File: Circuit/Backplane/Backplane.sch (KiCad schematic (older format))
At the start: 67 parts, among them CON1 peripheral_bridge, CON2 power_distributor, J1 USB_OTG, J2 power_source_mode, J3 general_power_source, J4 pneumatic, J5 pressure_sensor, J6 RS232_DVL, P1 imaging_sonar, P2 DVL, P3 computer1, P4 computer2, P5 ethernet_switch, P6 general, U1 LM1117-3.3, U2 TUSB4041I, U3 TLV73311PDBVT, Y1 24MHz

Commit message: grouping component in pcb
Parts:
- J2, J3: footprint Pin_Headers:Pin_Header_Straight_1x03_Pitch2.54mm -> Zeabus:90136-2013
- J5, J6: footprint Zeabus:70543-0002 -> Zeabus:90136-2013
- renumbered L2 to L1, L4 to L2, L5 to L3, L1 to L4, L3 to L5

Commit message: Change DVL Footprint
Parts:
- J2, J3, J5, J6: footprint Zeabus:90136-2013 -> Zeabus:70543-0002
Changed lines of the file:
@@
 F 0 "J6" H 9700 4900 50  0000 C CNN
 F 1 "RS232_DVL" H 9700 4500 50  0000 C CNN
-F 2 "Zeabus:90136-2013" H 9700 4700 50  0001 C CNN
+F 2 "Zeabus:70543-0002" H 9700 4700 50  0001 C CNN
 F 3 "" H 9700 4700 50  0001 C CNN
 	1    9700 4700
@@
 F 0 "J5" H 9700 4450 50  0000 C CNN
 F 1 "pressure_sensor" H 9700 4050 50  0000 C CNN
-F 2 "Zeabus:90136-2013" H 9700 4250 50  0001 C CNN
+F 2 "Zeabus:70543-0002" H 9700 4250 50  0001 C CNN
 F 3 "" H 9700 4250 50  0001 C CNN
 	1    9700 4250
@@
 F 0 "J2" H 1050 5900 50  0000 C CNN
 F 1 "power_source_mode" H 1050 5500 50  0000 C CNN
-F 2 "Zeabus:90136-2013" H 1100 5700 50  0001 C CNN
+F 2 "Zeabus:70543-0002" H 1100 5700 50  0001 C CNN
 F 3 "" H 1100 5700 50  0001 C CNN
 	1    1050 5700
@@
 F 0 "J3" H 1050 6700 50  0000 C CNN
 F 1 "general_power_source" H 1050 6300 50  0000 C CNN
-F 2 "Zeabus:90136-2013" H 1100 6500 50  0001 C CNN
+F 2 "Zeabus:70543-0002" H 1100 6500 50  0001 C CNN
 F 3 "" H 1100 6500 50  0001 C CNN
 	1    1050 6500

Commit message: Jumper Footprint change to pinheader
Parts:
- J2, J3: footprint Zeabus:70543-0002 -> Pin_Headers:Pin_Header_Straight_1x03_Pitch2.54mm
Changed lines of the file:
@@
 F 0 "J2" H 1050 5900 50  0000 C CNN
 F 1 "power_source_mode" H 1050 5500 50  0000 C CNN
-F 2 "Zeabus:70543-0002" H 1100 5700 50  0001 C CNN
+F 2 "Pin_Headers:Pin_Header_Straight_1x03_Pitch2.54mm" H 1100 5700 50  0001 C CNN
 F 3 "" H 1100 5700 50  0001 C CNN
 	1    1050 5700
@@
 F 0 "J3" H 1050 6700 50  0000 C CNN
 F 1 "general_power_source" H 1050 6300 50  0000 C CNN
-F 2 "Zeabus:70543-0002" H 1100 6500 50  0001 C CNN
+F 2 "Pin_Headers:Pin_Header_Straight_1x03_Pitch2.54mm" H 1100 6500 50  0001 C CNN
 F 3 "" H 1100 6500 50  0001 C CNN
 	1    1050 6500

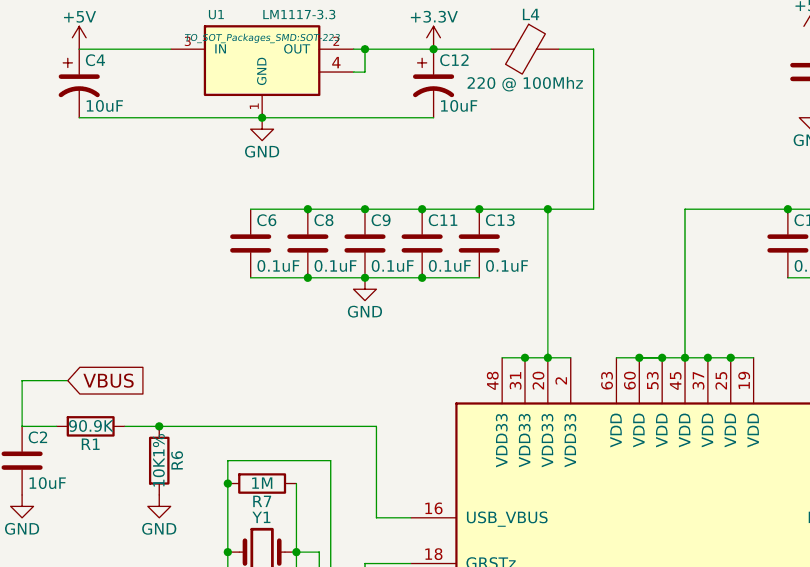
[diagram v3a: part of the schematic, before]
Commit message: changed value of capacitor that connected with VDD33 (0.1uF to 10uF)
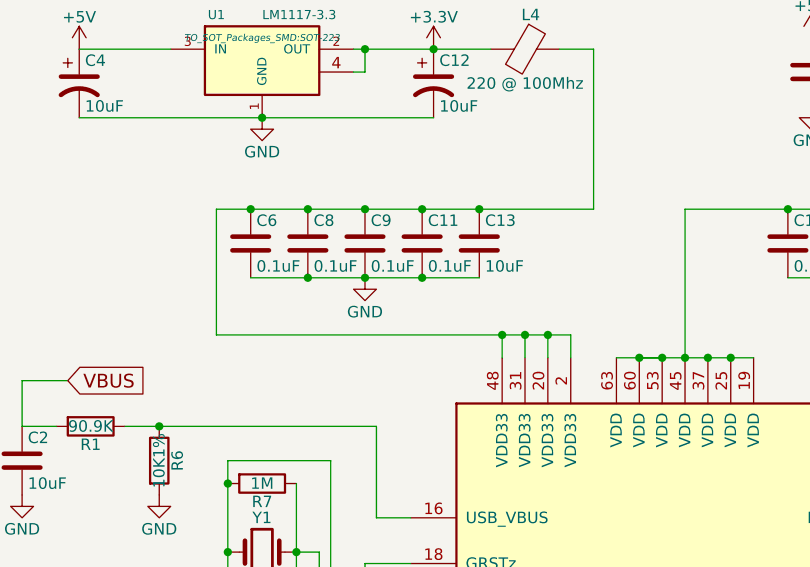
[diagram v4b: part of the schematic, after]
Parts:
- C13: value 0.1uF -> 10uF
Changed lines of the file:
@@
 P 3400 1850
 F 0 "C13" H 3425 1950 50  0000 L CNN
-F 1 "0.1uF" H 3425 1750 50  0000 L CNN
+F 1 "10uF" H 3425 1750 50  0000 L CNN
 F 2 "Capacitors_SMD:C_0603_HandSoldering" H 3438 1700 50  0001 C CNN
 F 3 "" H 3400 1850 50  0001 C CNN
@@
 	3100 3950 3100 4050
 Wire Wire Line
-	3500 2350 3800 2350
-Connection ~ 3600 2350
-Connection ~ 3700 2350
-Wire Wire Line
-	3700 1700 3700 2350
-Wire Wire Line
 	4000 2350 4600 2350
 Connection ~ 4100 2350
@@
 	4300 1700 4300 2350
 Wire Wire Line
-	2400 1700 3900 1700
+	2250 1700 3900 1700
 Connection ~ 2650 1700
 Connection ~ 2900 1700
@@
 Wire Wire Line
 	3900 1000 3900 1700
-Connection ~ 3700 1700
 Wire Wire Line
 	11050 1600 11250 1600
+Wire Wire Line
+	3800 2350 3800 2250
+Wire Wire Line
+	3800 2250 2250 2250
+Wire Wire Line
+	2250 2250 2250 1700
+Connection ~ 2400 1700
+Wire Wire Line
+	3700 2350 3700 2250
+Connection ~ 3700 2250
+Wire Wire Line
+	3600 2350 3600 2250
+Connection ~ 3600 2250
+Wire Wire Line
+	3500 2350 3500 2250
+Connection ~ 3500 2250
 $EndSCHEMATC

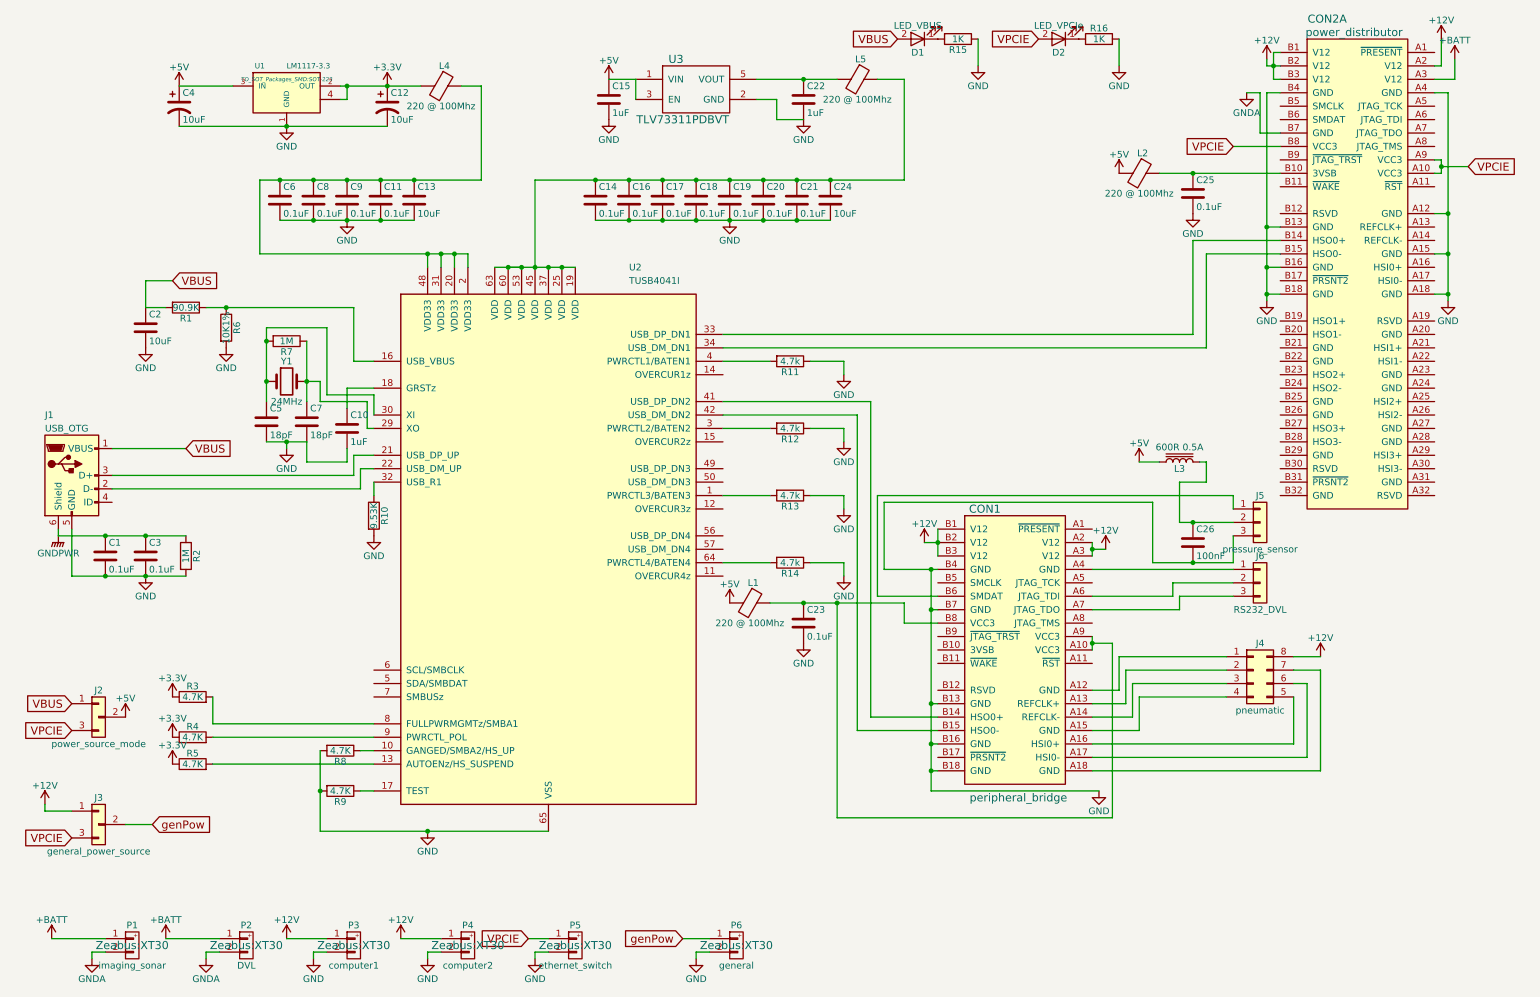
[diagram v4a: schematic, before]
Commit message: Add LEDS
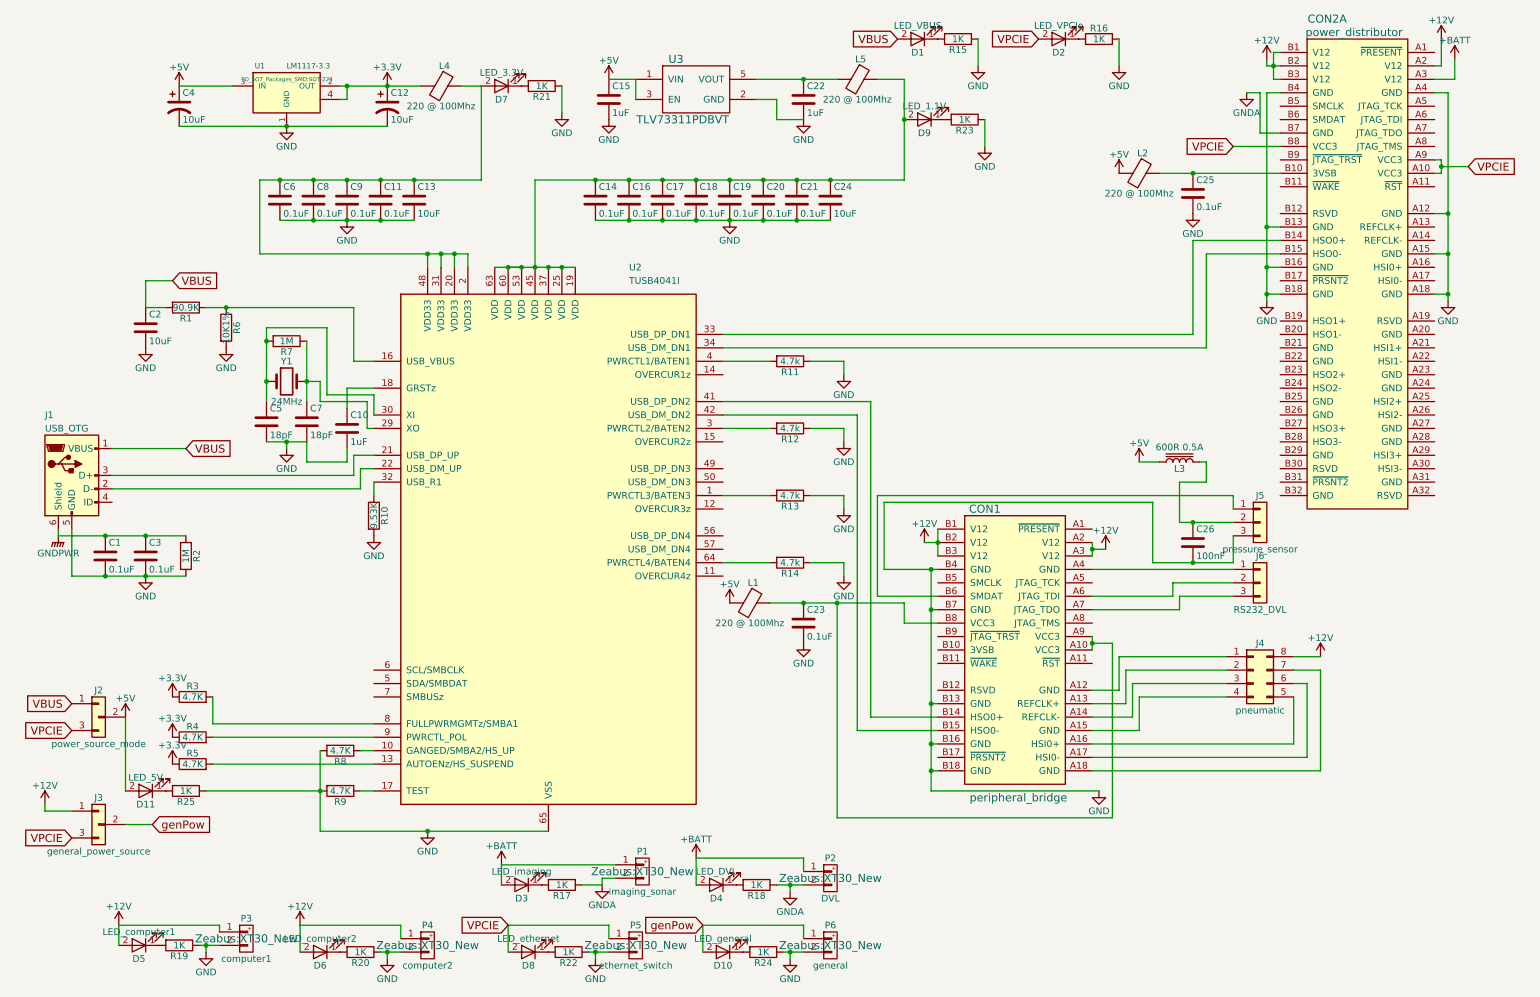
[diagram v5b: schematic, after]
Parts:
- added D10: LED_general, LEDs:LED_0603_HandSoldering, symbol LED
- added D11: LED_5V, LEDs:LED_0603_HandSoldering, symbol LED
- added D3: LED_imaging, LEDs:LED_0603_HandSoldering, symbol LED
- added D4: LED_DVL, LEDs:LED_0603_HandSoldering, symbol LED
- added D5: LED_computer1, LEDs:LED_0603_HandSoldering, symbol LED
- added D6: LED_computer2, LEDs:LED_0603_HandSoldering, symbol LED
- added D7: LED_3.3V, LEDs:LED_0603_HandSoldering, symbol LED
- added D8: LED_ethernet, LEDs:LED_0603_HandSoldering, symbol LED
- added D9: LED_1.1V, LEDs:LED_0603_HandSoldering, symbol LED
- added R17, R18, R19, R20, R21, R22, R23, R24, R25: 1K, Resistors_SMD:R_0603_HandSoldering, symbol R
- P1, P2, P3, P4, P5, P6: footprint Zeabus:XT30 -> Zeabus:XT30_New
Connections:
- net +12V: now also D5.2 (A), D6.2 (A)
- net +5V: now also D11.2 (A)
- net +BATT: now also D3.2 (A), D4.2 (A)
- net GND: now also R19.1, R20.1, R21.1, R22.1, R23.1, R24.1, R25.1
- net GNDA: now also R17.1, R18.1
- net VPCIE: now also D8.2 (A)
- net genPow: now also D10.2 (A)
- net at C14.1, C16.1, C17.1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: now also D9.2 (A)
- net at C11.1, C13.1, C6.1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: now also D7.2 (A)
- new net: D7.1 (K), R21.2
- new net: D9.1 (K), R23.2
- new net: D3.1 (K), R17.2
- new net: D5.1 (K), R19.2
- new net: D4.1 (K), R18.2
- new net: D6.1 (K), R20.2
- new net: D8.1 (K), R22.2
- new net: D10.1 (K), R24.2
- new net: D11.1 (K), R25.2
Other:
- moved on the sheet: P1, P2, P3, P4, P5, P6

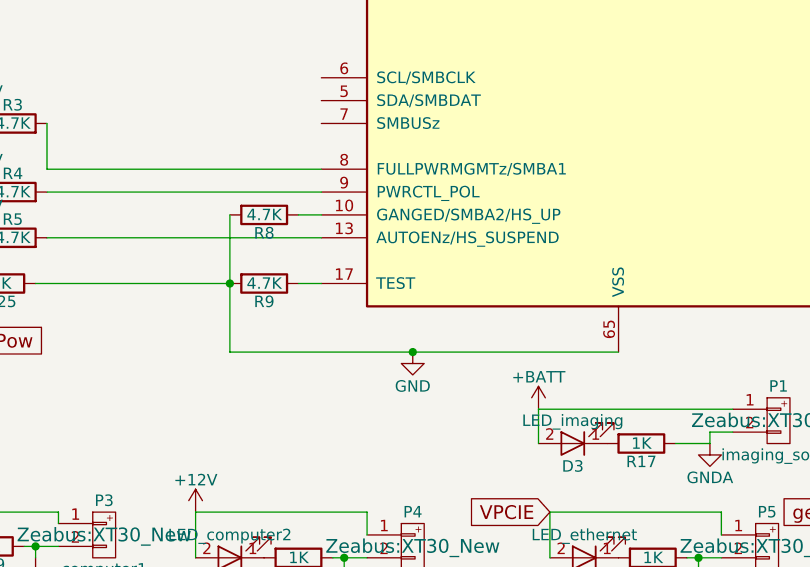
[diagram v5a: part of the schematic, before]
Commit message: relocated component in pcb
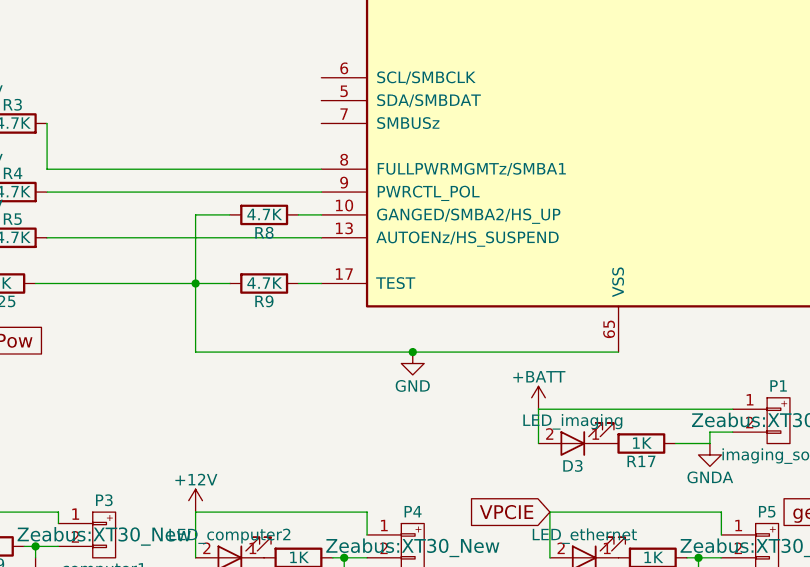
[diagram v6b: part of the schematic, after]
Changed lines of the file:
@@
 	6600 4550 6600 4650
 Wire Wire Line
-	2700 6550 4400 6550
+	2550 6550 4400 6550
 Wire Wire Line
 	3100 5950 3000 5950
@@
 	1900 5750 1900 5550
 Connection ~ 7250 4600
-Wire Wire Line
-	2700 5950 2700 6550
-Connection ~ 2700 6250
 Wire Wire Line
 	3100 3450 3100 3300
@@
 	1    0    0    -1
 $EndComp
+Wire Wire Line
+	2700 5950 2550 5950
+Wire Wire Line
+	2550 5950 2550 6550
+Connection ~ 2550 6250
 $EndSCHEMATC

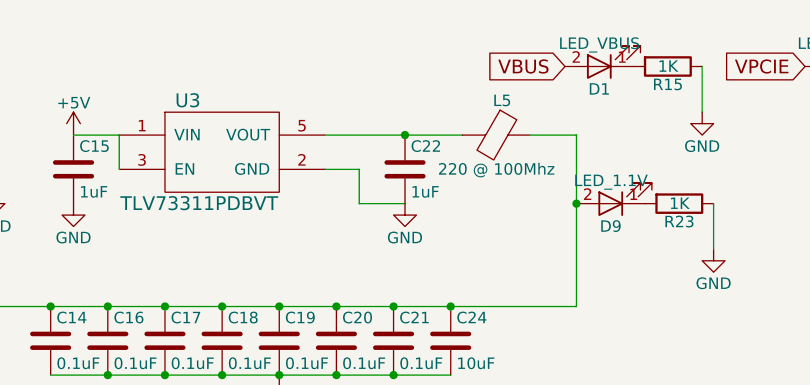
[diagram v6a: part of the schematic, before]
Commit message: connected all component
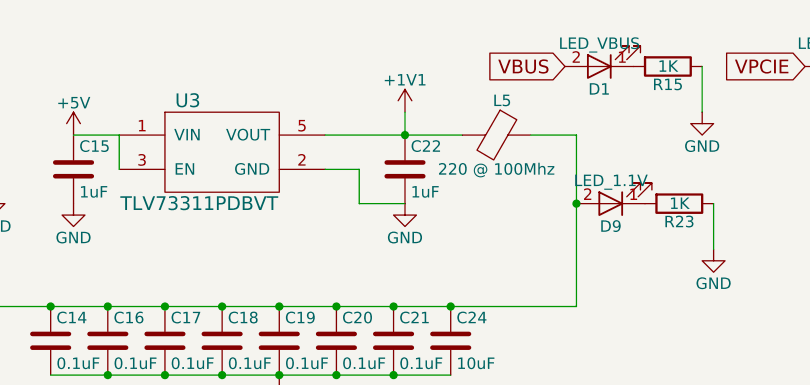
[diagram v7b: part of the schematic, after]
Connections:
- net +1V1: now reaches C22.1, L5.2, U3.5 (VOUT)
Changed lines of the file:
@@
 	2550 5950 2550 6550
 Connection ~ 2550 6250
+$Comp
+L +1V1 #PWR?
+U 1 1 5A6CF6AF
+P 6300 850
+F 0 "#PWR?" H 6300 700 50  0001 C CNN
+F 1 "+1V1" H 6300 990 50  0000 C CNN
+F 2 "" H 6300 850 50  0001 C CNN
+F 3 "" H 6300 850 50  0001 C CNN
+	1    6300 850
+	1    0    0    -1
+$EndComp
+Wire Wire Line
+	6300 950  6300 850
 $EndSCHEMATC

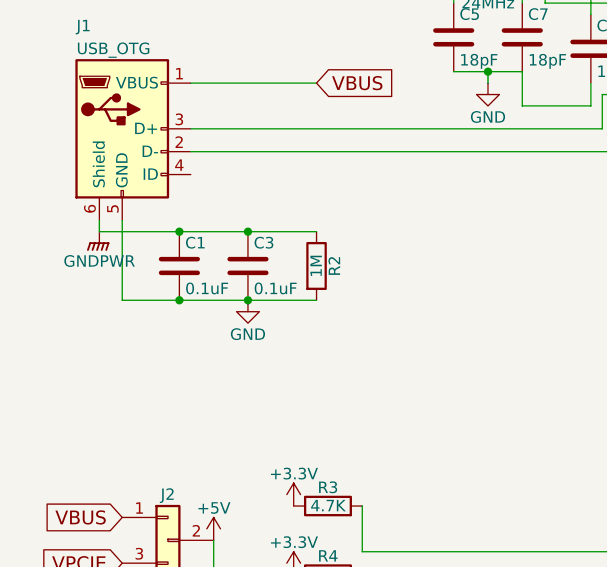
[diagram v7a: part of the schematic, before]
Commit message: change gndpwr to gnd at pin6(shield) in usb port
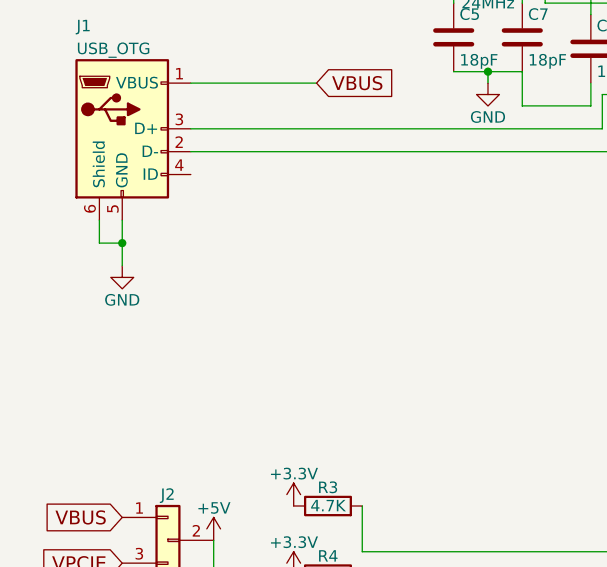
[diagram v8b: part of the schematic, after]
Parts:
- removed C1, C3: 0.1uF, Capacitors_SMD:C_0603_HandSoldering, symbol C
- removed R2: 1M, Resistors_SMD:R_0603_HandSoldering, symbol R
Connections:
- net GNDPWR is gone; now on net GND: J1.6 (Shield)
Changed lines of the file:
@@
-$EndComp
-$Comp
-L C C1
-U 1 1 5A565759
-P 1100 4500
-F 0 "C1" H 1125 4600 50  0000 L CNN
-F 1 "0.1uF" H 1125 4400 50  0000 L CNN
-F 2 "Capacitors_SMD:C_0603_HandSoldering" H 1138 4350 50  0001 C CNN
-F 3 "" H 1100 4500 50  0001 C CNN
-	1    1100 4500
-	1    0    0    -1
-$EndComp
-$Comp
-L C C3
-U 1 1 5A5657D2
-P 1400 4500
-F 0 "C3" H 1425 4600 50  0000 L CNN
-F 1 "0.1uF" H 1425 4400 50  0000 L CNN
-F 2 "Capacitors_SMD:C_0603_HandSoldering" H 1438 4350 50  0001 C CNN
-F 3 "" H 1400 4500 50  0001 C CNN
-	1    1400 4500
-	1    0    0    -1
-$EndComp
-$Comp
-L R R2
-U 1 1 5A565988
-P 1700 4500
-F 0 "R2" V 1780 4500 50  0000 C CNN
-F 1 "1M" V 1700 4500 50  0000 C CNN
-F 2 "Resistors_SMD:R_0603_HandSoldering" V 1630 4500 50  0001 C CNN
-F 3 "" H 1700 4500 50  0001 C CNN
-	1    1700 4500
-	1    0    0    -1
-$EndComp
-$Comp
-L GNDPWR #PWR2
-U 1 1 5A565F4A
-P 750 4350
-F 0 "#PWR2" H 750 4150 50  0001 C CNN
-F 1 "GNDPWR" H 750 4220 50  0000 C CNN
-F 2 "" H 750 4300 50  0001 C CNN
-F 3 "" H 750 4300 50  0001 C CNN
-	1    750  4350
-	1    0    0    -1
-$EndComp
-$Comp
-L GND #PWR6
-U 1 1 5A565F9E
-P 1400 4650
-F 0 "#PWR6" H 1400 4400 50  0001 C CNN
-F 1 "GND" H 1400 4500 50  0000 C CNN
-F 2 "" H 1400 4650 50  0001 C CNN
-F 3 "" H 1400 4650 50  0001 C CNN
-	1    1400 4650
-	1    0    0    -1
 $EndComp
 $Comp
@@
 	3000 4000 1150 4000
 Wire Wire Line
-	750  4350 1700 4350
-Connection ~ 1100 4350
-Wire Wire Line
-	850  4650 1700 4650
-Connection ~ 1100 4650
-Connection ~ 1400 4350
-Connection ~ 1400 4650
-Wire Wire Line
-	750  4300 750  4350
-Wire Wire Line
-	850  4300 850  4650
-Wire Wire Line
 	3100 3950 3100 4050
 Wire Wire Line
@@
 Wire Wire Line
 	6300 950  6300 850
+Wire Wire Line
+	750  4300 750  4400
+Wire Wire Line
+	750  4400 850  4400
+Wire Wire Line
+	850  4300 850  4500
+Connection ~ 850  4400
+$Comp
+L GND #PWR?
+U 1 1 5A6DFFC1
+P 850 4500
+F 0 "#PWR?" H 850 4250 50  0001 C CNN
+F 1 "GND" H 850 4350 50  0000 C CNN
+F 2 "" H 850 4500 50  0001 C CNN
+F 3 "" H 850 4500 50  0001 C CNN
+	1    850  4500
+	1    0    0    -1
+$EndComp
 $EndSCHEMATC
